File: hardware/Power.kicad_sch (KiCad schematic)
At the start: 20 parts, among them IC101 nPM1300-QEXX, X101 BATTERY

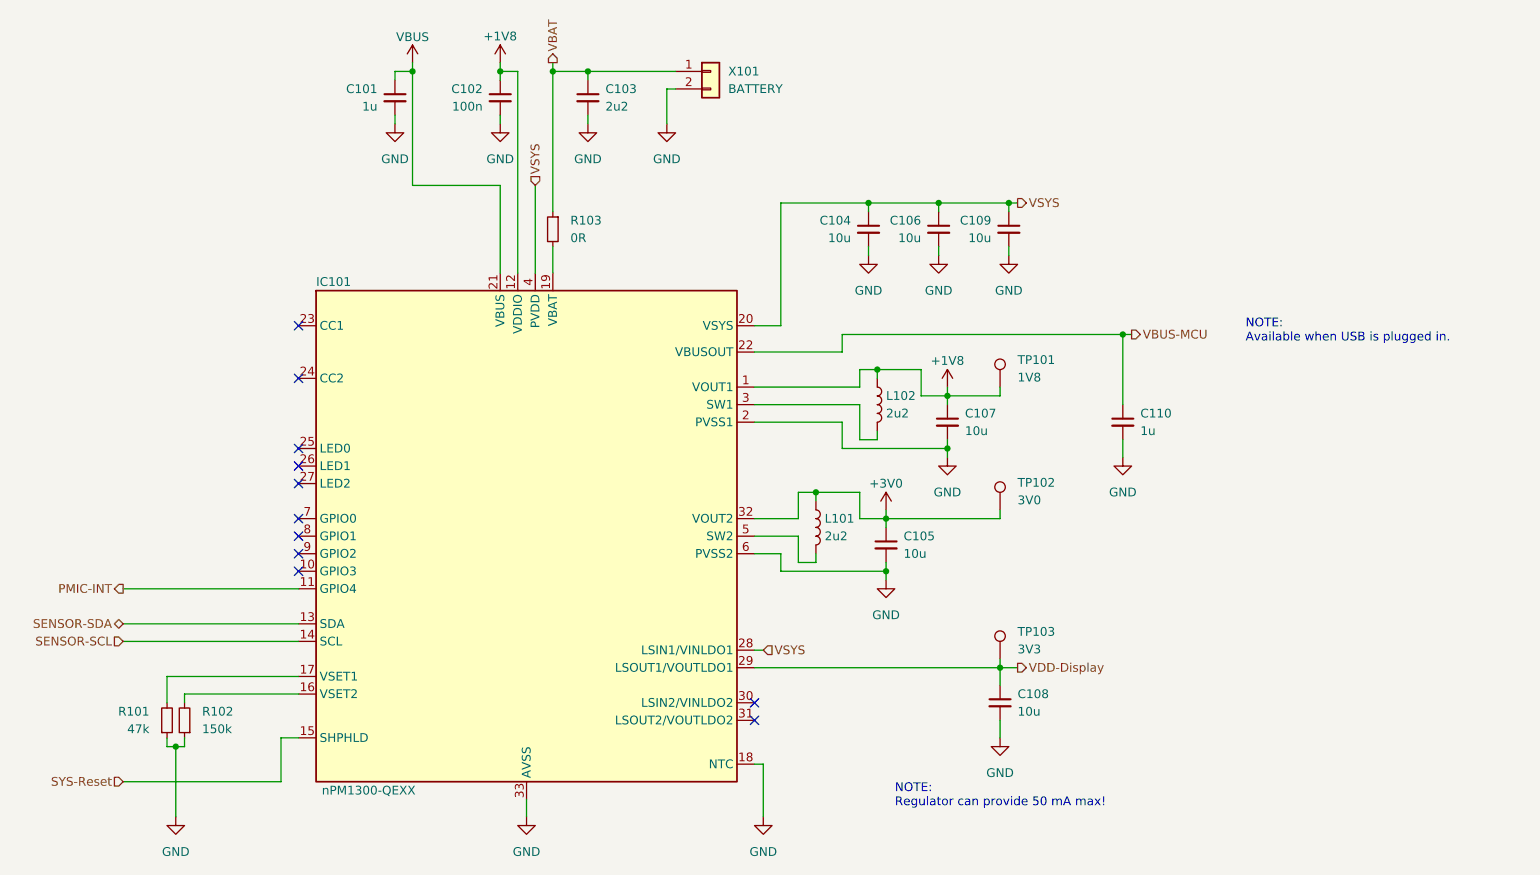
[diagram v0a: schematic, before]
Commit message: KiBot: Enhance KiBot configuration
- Implement #110
- Implement #109
- Add refresh for PCB specifications
- Add refresh for stackup

Signed-off-by: Daniel Kampert <danielkampert@kampis-elektroecke.de>
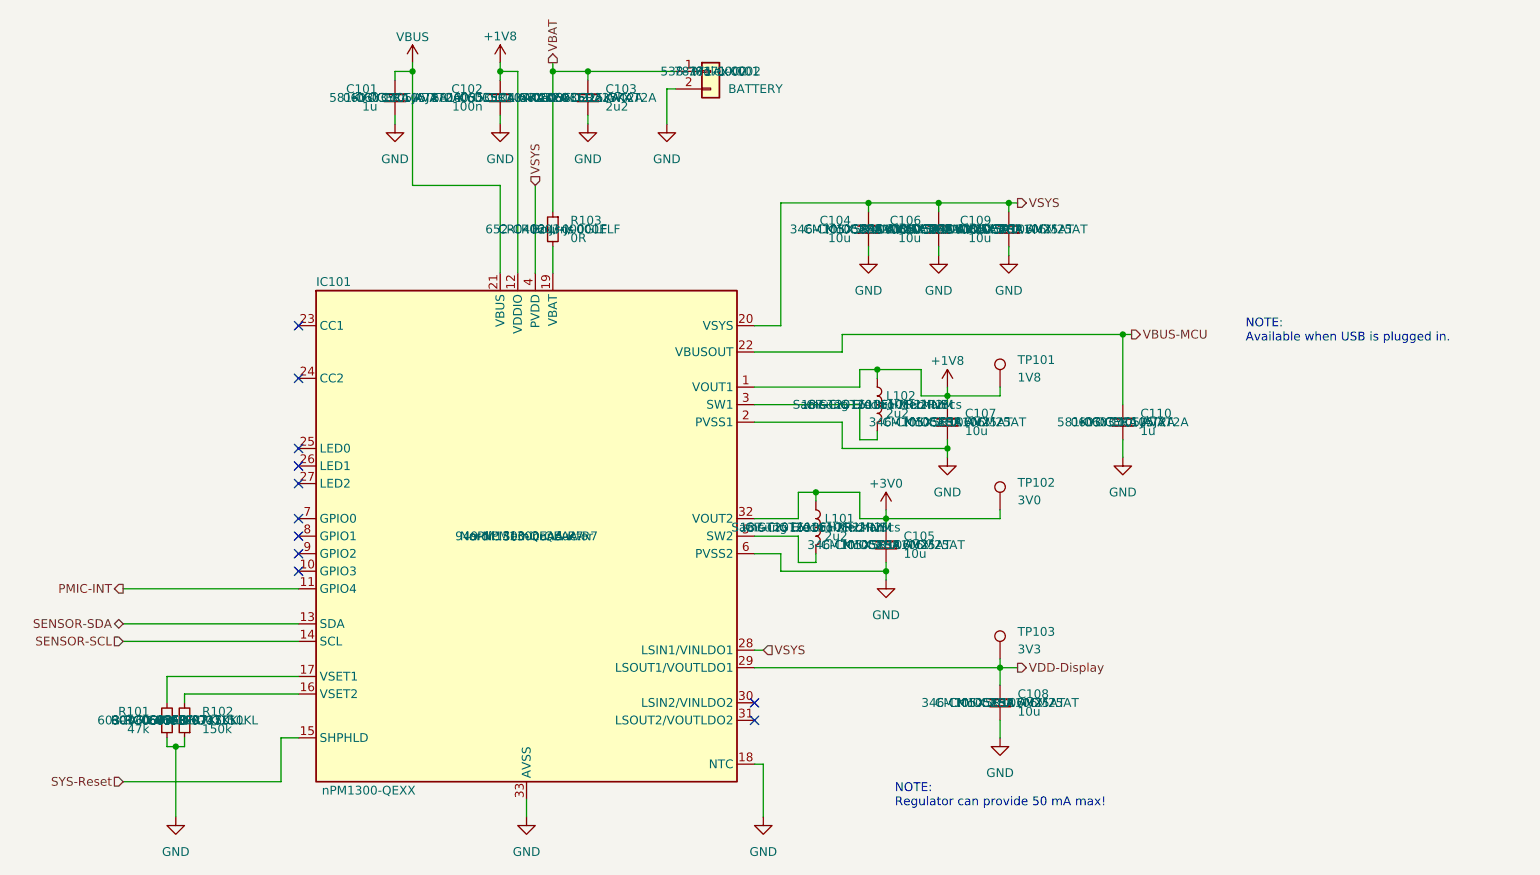
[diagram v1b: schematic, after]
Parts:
- C101, C110: Mfr. KYOCERA AVX -> (none); Mfr. No. 0603YC105JAT2A -> (none); Order Number 581-0603YC105JAT2A -> (none); manf (none) -> KYOCERA AVX; manf# (none) -> 0603YC105JAT2A; mouser# (none) -> 581-0603YC105JAT2A
- C102: Mfr. KYOCERA AVX -> (none); Mfr. No. 06035C104KAT2A -> (none); Order Number 581-06035C104KAT2A -> (none); manf (none) -> KYOCERA AVX; manf# (none) -> 06035C104KAT2A; mouser# (none) -> 581-06035C104KAT2A
- C103: Mfr. KYOCERA AVX -> (none); Mfr. No. 06036D225KAT2A -> (none); Order Number 581-06036D225KAT2A -> (none); manf (none) -> KYOCERA AVX; manf# (none) -> 06036D225KAT2A; mouser# (none) -> 581-06036D225KAT2A
- C104, C105, C106, C107, C108, C109: Mfr. KYOCERA AVX -> (none); Mfr. No. CM105X5R106M25AT -> (none); Order Number 346-CM105X5R106M25AT -> (none); manf (none) -> KYOCERA AVX; manf# (none) -> CM105X5R106M25AT; mouser# (none) -> 346-CM105X5R106M25AT
- IC101: Mfr. Nordic Semiconductor -> (none); Mfr. No. nPM1300-QEAA-R7 -> (none); Order Number 949-NPM1300-QEAA-R7 -> (none); manf (none) -> Nordic Semiconductor; manf# (none) -> nPM1300-QEAA-R7; mouser# (none) -> 949-NPM1300-QEAA-R7
- L101, L102: Mfr. Samsung Electro-Mechanics -> (none); Mfr. No. CIGT201610EH2R2MNE -> (none); Order Number 187-CIGT201610EH2R2M -> (none); manf (none) -> Samsung Electro-Mechanics; manf# (none) -> CIGT201610EH2R2MNE; mouser# (none) -> 187-CIGT201610EH2R2M
- R101: Mfr. YAGEO -> (none); Mfr. No. RC0603FR-0747KL -> (none); Order Number 603-RC0603FR-0747KL -> (none); manf (none) -> YAGEO; manf# (none) -> RC0603FR-0747KL; mouser# (none) -> 603-RC0603FR-0747KL
- R102: Mfr. YAGEO -> (none); Mfr. No. RC0603FR-07150KL -> (none); Order Number 603-RC0603FR-07150KL -> (none); manf (none) -> YAGEO; manf# (none) -> RC0603FR-07150KL; mouser# (none) -> 603-RC0603FR-07150KL
- R103: Mfr. Bourns -> (none); Mfr. No. CR0402-J/-000GLF -> (none); Order Number 652-CR0603-J/-000ELF -> (none); manf (none) -> Bourns; manf# (none) -> CR0402-J/-000GLF; mouser# (none) -> 652-CR0603-J/-000ELF
- X101: Mfr. Molex -> (none); Mfr. No. 78171-0002 -> (none); Order Number 538-78171-0002 -> (none); manf (none) -> Molex; manf# (none) -> 78171-0002; mouser# (none) -> 538-78171-0002
